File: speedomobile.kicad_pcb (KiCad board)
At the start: 4 copper layers, 100 x 100 mm, 137 parts, among them J1 Conn_01x04, J10 Conn_02x02_Odd_Even, J11 Conn_02x02_Odd_Even, J12 Conn_02x02_Odd_Even, J13 Conn_02x02_Odd_Even, J14 Conn_02x02_Odd_Even, J15 Conn_02x02_Odd_Even, J16 Conn_02x02_Odd_Even, J17 Conn_02x02_Odd_Even, J18 Conn_01x02, J19 Conn_01x02, J2 Conn_01x04, J20 Conn_01x03, J21 Conn_01x03, J22 Conn_01x07, J23 Conn_01x04, J24 Conn_01x03, J25 Conn_01x03, J26 Conn_01x03, J27 Conn_01x02, J28 Conn_01x06, J29 Conn_01x02, J3 Conn_01x04, J30 Conn_01x06, J31 Conn_02x06_Odd_Even, J32 Conn_01x02, J33 Conn_01x03, J34 Conn_01x02, J35 SDCARD_breakout, J36 Conn_01x03, J37 Conn_01x02, J38 Conn_01x03, J4 Conn_01x04, J5 Conn_01x04, J6 Conn_01x04, J7 Conn_01x07, J8 Conn_01x04, J9 Conn_Coaxial, Q1 DMT6012LSS, Q2 DMT6012LSS, Q3 DMT6012LSS, Q4 DMT6012LSS, Q5 BSS138, Q6 BSS138, SW1 SW_Push, U1 MCP1501-33xCH, U10 NEO-M9N, U11 PCF8574, U12 PCF8574, U13 TCA9617A, U2 SC0918, U3 74AHCT367, U4 BTS4140N, U5 CD74HC4067M, U6 MCS1802, U7 MCS1802, U8 V48SD, U9 adafruit_LSM9DS1

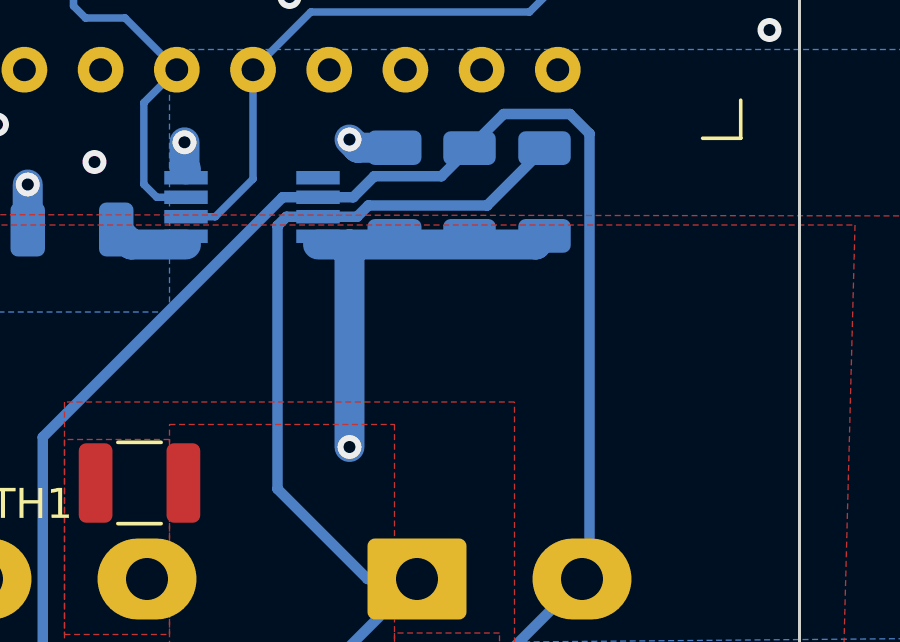
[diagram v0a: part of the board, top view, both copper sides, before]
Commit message: switching to 3v3 i2c
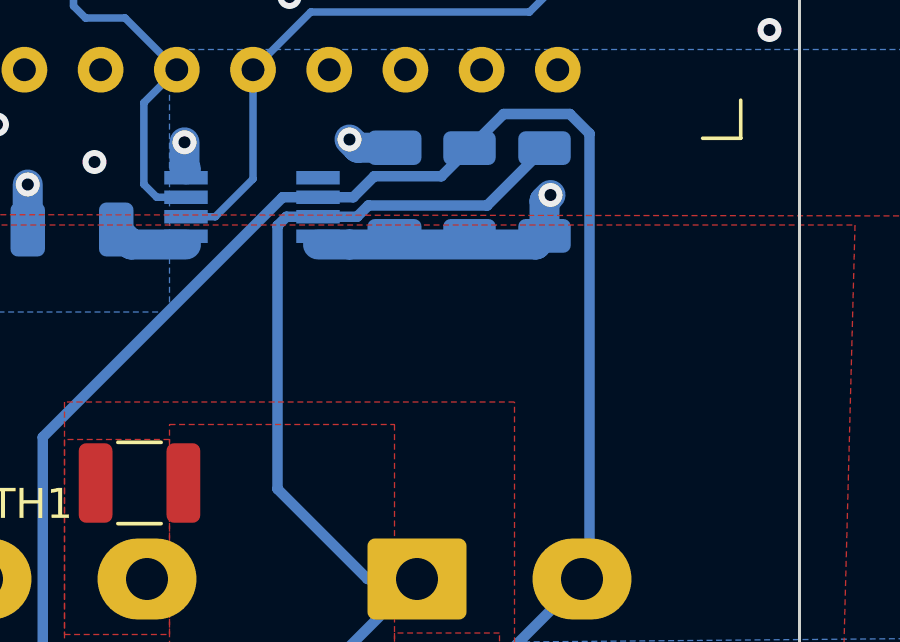
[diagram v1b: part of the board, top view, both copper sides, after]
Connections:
- C24 pad 1: +5V -> +3V3
- R1 pad 1: +5V -> +3V3
- R29 pad 1: +5V -> +3V3
- U13 pad 8: +5V -> +3V3
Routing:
- net +5V: track 21.3 -> 6.87 mm, vias 1 -> 0
- net +3V3: track 219.2 -> 228.3 mm, vias 121 -> 122
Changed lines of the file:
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@@
       (stroke (width 0.1) (type solid)) (layer "B.Fab"))
     (pad "1" smd roundrect (at -1.475 0 90) (size 1.15 1.8) (layers "B.Cu" "B.Paste" "B.Mask") (roundrect_rratio 0.217391)
-      (net 1 "+5V") (pintype "passive"))
+      (net 7 "+3V3") (pintype "passive"))
     (pad "2" smd roundrect (at 1.475 0 90) (size 1.15 1.8) (layers "B.Cu" "B.Paste" "B.Mask") (roundrect_rratio 0.217391)
       (net 6 "GND") (pintype "passive"))
@@
       (stroke (width 0.1) (type solid)) (layer "B.Fab"))
     (pad "1" smd roundrect (at -1.4625 0 90) (size 1.125 1.75) (layers "B.Cu" "B.Paste" "B.Mask") (roundrect_rratio 0.222222)
-      (net 1 "+5V") (pintype "passive"))
+      (net 7 "+3V3") (pintype "passive"))
     (pad "2" smd roundrect (at 1.4625 0 90) (size 1.125 1.75) (layers "B.Cu" "B.Paste" "B.Mask") (roundrect_rratio 0.222222)
       (net 106 "/I2C devices/led ribbon/FAST_SCL_5V") (pintype "passive"))
@@
       (stroke (width 0.1) (type solid)) (layer "B.Fab"))
     (pad "1" smd roundrect (at -1.4625 0 90) (size 1.125 1.75) (layers "B.Cu" "B.Paste" "B.Mask") (roundrect_rratio 0.222222)
-      (net 1 "+5V") (pintype "passive"))
+      (net 7 "+3V3") (pintype "passive"))
     (pad "2" smd roundrect (at 1.4625 0 90) (size 1.125 1.75) (layers "B.Cu" "B.Paste" "B.Mask") (roundrect_rratio 0.222222)
       (net 137 "/I2C devices/led ribbon/FAST_SDA_5V") (pintype "passive"))
@@
       (net 106 "/I2C devices/led ribbon/FAST_SCL_5V") (pinfunction "SCLB") (pintype "bidirectional"))
     (pad "8" smd rect (at 2.2 0.975 90) (size 0.45 1.45) (layers "B.Cu" "B.Paste" "B.Mask")
-      (net 1 "+5V") (pinfunction "VCCB") (pintype "power_in"))
+      (net 7 "+3V3") (pinfunction "VCCB") (pintype "power_in"))
     (model "${KICAD6_3DMODEL_DIR}/Package_SO.3dshapes/VSSOP-8_3.0x3.0mm_P0.65mm.wrl"
       (offset (xyz 0 0 0))
@@
   )
   (segment (start 145.542 110.236) (end 142.367002 110.236) (width 2.2) (layer "F.Cu") (net 1))
-  (via (at 170 69) (size 0.8) (drill 0.4) (layers "F.Cu" "B.Cu") (net 1))
   (segment (start 141.866 110.0035) (end 142.1345 110.0035) (width 1) (layer "B.Cu") (net 1))
   (segment (start 141.3 107.1375) (end 141.3 109.4375) (width 1) (layer "B.Cu") (net 1))
-  (segment (start 170 62.25) (end 168.95 62.25) (width 1) (layer "B.Cu") (net 1))
   (segment (start 141.3 109.4375) (end 141.866 110.0035) (width 1) (layer "B.Cu") (net 1))
-  (segment (start 170 69) (end 170 62.25) (width 1) (layer "B.Cu") (net 1))
   (segment (start 142.367002 110.236) (end 142.240002 110.109) (width 2.2) (layer "B.Cu") (net 1))
   (segment (start 142.1345 110.0035) (end 142.24 110.109) (width 1) (layer "B.Cu") (net 1))
-  (segment (start 176.5 61.9625) (end 176.2125 62.25) (width 1) (layer "B.Cu") (net 1))
-  (segment (start 176.2125 62.25) (end 170 62.25) (width 1) (layer "B.Cu") (net 1))
   (segment (start 120.16 45.63) (end 118.5 45.63) (width 0.25) (layer "B.Cu") (net 2))
   (segment (start 118.5 45.63) (end 115.49 42.62) (width 0.25) (layer "B.Cu") (net 2))
@@
   (via (at 168.1 43.4) (size 0.8) (drill 0.4) (layers "F.Cu" "B.Cu") (net 7))
   (via (at 161.5 59.5) (size 0.8) (drill 0.4) (layers "F.Cu" "B.Cu") (net 7))
+  (via (at 176.7 60.6) (size 0.8) (drill 0.4) (layers "F.Cu" "B.Cu") (net 7))
   (via (at 183.3 52.4) (size 0.8) (drill 0.4) (layers "F.Cu" "B.Cu") (net 7))
   (via (at 153.4 37.9) (size 0.8) (drill 0.4) (layers "F.Cu" "B.Cu") (net 7))
@@
   (via (at 159.5 32.9) (size 0.8) (drill 0.4) (layers "F.Cu" "B.Cu") (net 7))
   (segment (start 132.193621 42.7) (end 134.086828 42.7) (width 0.5) (layer "B.Cu") (net 7))
+  (segment (start 176.5 60.8) (end 176.7 60.6) (width 1) (layer "B.Cu") (net 7))
   (segment (start 122.301 66.04) (end 123.276 66.04) (width 1.8) (layer "B.Cu") (net 7))
   (segment (start 121.329 88.184) (end 120.219625 87.074625) (width 1.8) (layer "B.Cu") (net 7))
@@
   (segment (start 135.025 43.638172) (end 135.025 47.675) (width 0.5) (layer "B.Cu") (net 7))
   (segment (start 107.2 49.2) (end 107.2 46.2) (width 1.8) (layer "B.Cu") (net 7))
+  (segment (start 176.5 61.9625) (end 176.5 60.8) (width 1) (layer "B.Cu") (net 7))
   (segment (start 107.2 46.2) (end 106.6 45.6) (width 1.8) (layer "B.Cu") (net 7))
   (segment (start 108.75 40.25) (end 108.75 40) (width 1.8) (layer "B.Cu") (net 7))
@@
   (segment (start 108.75 41.467284) (end 108.75 40.25) (width 1.8) (layer "B.Cu") (net 7))
   (segment (start 123.276 66.04) (end 128.204 61.112) (width 1.8) (layer "B.Cu") (net 7))
+  (segment (start 170 62.25) (end 168.95 62.25) (width 1) (layer "B.Cu") (net 7))
   (segment (start 135.025 47.675) (end 133.4 49.3) (width 0.5) (layer "B.Cu") (net 7))
   (segment (start 96.46 63.545) (end 95.03 64.975) (width 0.5) (layer "B.Cu") (net 7))
@@
   (segment (start 106 103.4) (end 106 109.8) (width 1.8) (layer "B.Cu") (net 7))
   (segment (start 97.71 52.78) (end 98.42 52.78) (width 1.8) (layer "B.Cu") (net 7))
+  (segment (start 176.5 61.9625) (end 176.2125 62.25) (width 1) (layer "B.Cu") (net 7))
   (segment (start 94.7 95.2) (end 96.025 93.875) (width 1.8) (layer "B.Cu") (net 7))
   (segment (start 106.6 43.617284) (end 108.75 41.467284) (width 1.8) (layer "B.Cu") (net 7))
   (segment (start 91.2 95.2) (end 94.7 95.2) (width 1.8) (layer "B.Cu") (net 7))
+  (segment (start 176.2125 62.25) (end 170 62.25) (width 1) (layer "B.Cu") (net 7))
   (segment (start 141.975 52.95) (end 141.975 50.686918) (width 0.5) (layer "B.Cu") (net 7))
   (segment (start 162.225 61.75) (end 162.725 62.25) (width 1) (layer "B.Cu") (net 7))

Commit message: JLCJLCJLCJLC
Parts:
- removed Q5, Q6: BSS138, Package_TO_SOT_SMD:SOT-23
- removed R21, R22: 4k7, Resistor_SMD:R_1206_3216Metric
- added J39: Conn_02x02_Odd_Even, Connector_Molex:Molex_Mini-Fit_Jr_5566-04A_2x02_P4.20mm_Vertical, B.Cu at (172.3, 65.6)
- added TH4: 7,5A, Resistor_SMD:R_1210_3225Metric, F.Cu at (167.4, 68.3)
- added TH6: 7,5A, Resistor_SMD:R_1210_3225Metric, F.Cu at (172.5, 73.1)
- J36: value Conn_01x03 -> Conn_02x02_Odd_Even; footprint Connector_PinHeader_2.54mm:PinHeader_1x03_P2.54mm_Vertical -> Connector_Molex:Molex_Mini-Fit_Jr_5566-04A_2x02_P4.20mm_Vertical
- J5: value Conn_01x04 -> Conn_01x05; footprint Connector_JST:JST_XH_B4B-XH-A_1x04_P2.50mm_Vertical -> Connector_JST:JST_XH_B5B-XH-A_1x05_P2.50mm_Vertical
- NT3, NT4: footprint NetTie:NetTie-2_SMD_Pad2.0mm -> additional:NetTie-2_SMD_Pad2.0mm-3,6mm
- TH10, TH11, TH12, TH13, TH9: footprint Resistor_SMD:R_1812_4532Metric -> Resistor_SMD:R_1210_3225Metric
- moved J36 75.2 mm to (163.3, 69.8), turned to 90 degrees
- moved J6 12.5 mm to (90.5, 42.8)
- moved C16 10.3 mm to (140.7, 103.5)
- moved J5 7.28 mm to (90.5, 56.2), turned to -90 degrees
- moved TH11 4.91 mm to (158.3, 122.1)
- moved TH12 4.34 mm to (165.5, 122.1)
- moved J10 2.99 mm to (163.2, 80.6)
- moved J11 2.99 mm to (163.2, 91.3)
- moved J12 2.99 mm to (163.2, 101.9)
- moved J13 2.99 mm to (163.2, 112.6)
- moved J15 2.99 mm to (172.2, 87.0)
- moved J17 2.99 mm to (172.2, 108.3)
- moved TH16 2.99 mm to (172.5, 94.6)
- moved TH18 2.99 mm to (172.5, 105.4)
- moved TH3 2.99 mm to (163.0, 83.9)
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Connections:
- J36 pad 1: GND -> /I2C devices/led ribbon/FAST_SCL_5V
- J36 pad 2: GND -> /I2C devices/led ribbon/LED9
- J36 pad 3: Net-(J36-Pin_3) -> /I2C devices/led ribbon/FAST_SDA_5V
- J5 pad 1: +3V3 -> +5VL
- J5 pad 2: /FAST_SDA -> +3V3
- J5 pad 3: /FAST_SCL -> /SDA
- J5 pad 4: GND -> /SCL
- J6 pad 1: +5VL -> +3V3
- J6 pad 2: /I2C devices/SDA_5V -> /SDA
- J6 pad 3: /I2C devices/SCL_5V -> /SCL
- U2 pad 37: Net-(J36-Pin_3) -> unconnected-(U2-3V3_EN-Pad37)
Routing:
- net +3V3: track 228.3 -> 177.2 mm, vias 122 -> 119
- net /SCL: track 140.6 -> 173.7 mm, vias 4 -> 2
- net /SDA: track 135.4 -> 163.7 mm, vias 4 -> 2
- net /FAST_SCL: track 181.0 -> 154.0 mm
- net Net-(J36-Pin_3): track 24.5 -> 0.00 mm
- net /FAST_SDA: track 167.4 -> 143.2 mm
- net /I2C devices/led ribbon/FAST_SDA_5V: track 122.8 -> 137.0 mm
- net /I2C devices/SCL_5V: track 9.72 -> 0.00 mm
- net /I2C devices/SDA_5V: track 9.29 -> 0.00 mm
- net /I2C devices/led ribbon/FAST_SCL_5V: track 102.6 -> 111.1 mm
- net /power/PWR2_PWM_ON: track 42.6 -> 37.3 mm, vias 1 -> 0
- net /UART: track 71.7 -> 75.5 mm, vias 0 -> 2
- net /ADC: track 58.3 -> 54.5 mm, vias 3 -> 1
- net +5V: track 6.87 -> 9.71 mm, vias 0 -> 7
- net /power/PWR1_PWM_ON: track 30.4 -> 27.7 mm
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- added copper zone on F.Cu, net /I2C devices/led ribbon/LED10
- added copper zone on F.Cu, net /I2C devices/led ribbon/LED9
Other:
- board text added: "5V-7.5A I2C"
- board text added: "5V40A"
- board text added: "I2C Expansion"
- board text added: "JLCJLCJLCJLC"
- board text added: "LCD+RFID"
- board text removed: "5V 40A"
- board text removed: "5V-3A I2C"
- board text removed: "LCD"
- board text removed: "RFID"

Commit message: 2 layers!
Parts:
- removed NT1: NetTie_2, NetTie:NetTie-2_SMD_Pad0.5mm
- removed NT3, NT4: NetTie_2, additional:NetTie-2_SMD_Pad2.0mm-3,6mm
- removed Q3, Q4: DMT6012LSS, Package_SO:SOIC-8_3.9x4.9mm_P1.27mm
- removed R14, R15: 1k, Resistor_SMD:R_1206_3216Metric
- removed R16, R17: 190k, Resistor_SMD:R_1206_3216Metric
- C13, C15, C16: moved to B.Cu
- J20, J21: value Conn_01x03 -> Conn_01x02; footprint Connector_JST:JST_XH_B3B-XH-A_1x03_P2.50mm_Vertical -> Connector_JST:JST_XH_B2B-XH-A_1x02_P2.50mm_Vertical
- moved R2 29.1 mm to (118.8, 69.3)
- moved D1 27.9 mm to (131.9, 101.7), turned to 45 degrees
- moved C13 17.9 mm to (129.1, 113.5), turned to -90 degrees
- moved C15 17.9 mm to (132.6, 113.5), turned to -90 degrees
- moved C16 17.9 mm to (125.8, 113.5), turned to -90 degrees
- moved J29 16.9 mm to (136.8, 126.9), turned to 90 degrees
- moved R6 11.6 mm to (117.3, 121.1), turned to 90 degrees
- moved Q1 10.2 mm to (134.3, 118.6)
- moved J27 9.63 mm to (151.0, 94.1)
- moved Q2 9.57 mm to (123.0, 126.2)
- moved R7 9.22 mm to (121.8, 110.6)
- moved R4 9.20 mm to (131.6, 123.7), turned to 90 degrees
- moved R3 8.98 mm to (129.3, 125.5), turned to -90 degrees
- moved R5 7.69 mm to (119.6, 121.1), turned to -90 degrees
- moved J21 7.53 mm to (154.7, 123.2)
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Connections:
- J10 pad 4: GNDPWR -> GND
- J11 pad 4: GNDPWR -> GND
- J12 pad 4: GNDPWR -> GND
- J13 pad 4: GNDPWR -> GND
- J14 pad 4: GNDPWR -> GND
- J15 pad 4: GNDPWR -> GND
- J16 pad 4: GNDPWR -> GND
- J17 pad 4: GNDPWR -> GND
- J18 pad 2: GNDPWR -> GND
- J19 pad 2: GNDPWR -> GND
- J20 pad 1: /power/PWR2 -> /power/PWR1
- J20 pad 2: /power/PWR2_PWM_ON -> GND
- J21 pad 1: /power/PWR1 -> /power/PWR2
- J21 pad 2: /power/PWR1_PWM_ON -> GND
- J31 pad 2: /GPIO0 -> GND
- J31 pad 3: /GPIO1 -> /GPIO0
- J31 pad 4: /GPIO2 -> /GPIO1
- J31 pad 5: /GPIO3 -> /GPIO2
- J31 pad 6: GND -> /GPIO3
- J36 pad 4: GNDPWR -> GND
- J39 pad 4: GNDPWR -> GND
- U2 pad 26: /PWR2_PWM -> unconnected-(U2-I2C0SDA/GP20-Pad26)
- U2 pad 27: /PWR1_PWM -> unconnected-(U2-I2C0SCL/GP21-Pad27)
- U8 pad 7: Net-(U8-Sense+) -> +5VL
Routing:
- net +3V3: track 177.2 -> 446.1 mm, vias 119 -> 7
- net /PWR2_PWM: track 99.3 -> 0.00 mm
- net /PWR1_PWM: track 97.6 -> 0.00 mm, vias 1 -> 0
- net +5VL: track 178.2 -> 249.5 mm, vias 4 -> 3
- net /power/PWR2_PWM_ON: track 37.3 -> 0.00 mm
- net /TSDZ2_RX: track 72.5 -> 106.4 mm
- net /TSDZ2_RX_5V: track 36.6 -> 3.27 mm
- net /power/PWR1_PWM_ON: track 27.7 -> 0.00 mm
- net Net-(Q4-G): track 18.3 -> 0.00 mm
- net +5V: track 9.71 -> 26.9 mm, vias 7 -> 5
- net +48V: track 26.0 -> 42.6 mm
- net Net-(Q3-G): track 14.3 -> 0.00 mm
- net Net-(U8-Sense+): track 13.0 -> 0.00 mm
- net /FAST_SDA: track 143.2 -> 155.1 mm, vias 1 -> 3
- net Net-(Q1-G): track 7.24 -> 19.1 mm
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- removed copper zone on B.Cu, net +5VL
- removed copper zone on In1.Cu, net GND
- removed copper zone on In2.Cu, net GND
- removed copper zone on B.Cu, net GNDPWR
- removed copper zone on F.Cu, net GNDPWR
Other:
- copper layers 4 -> 2

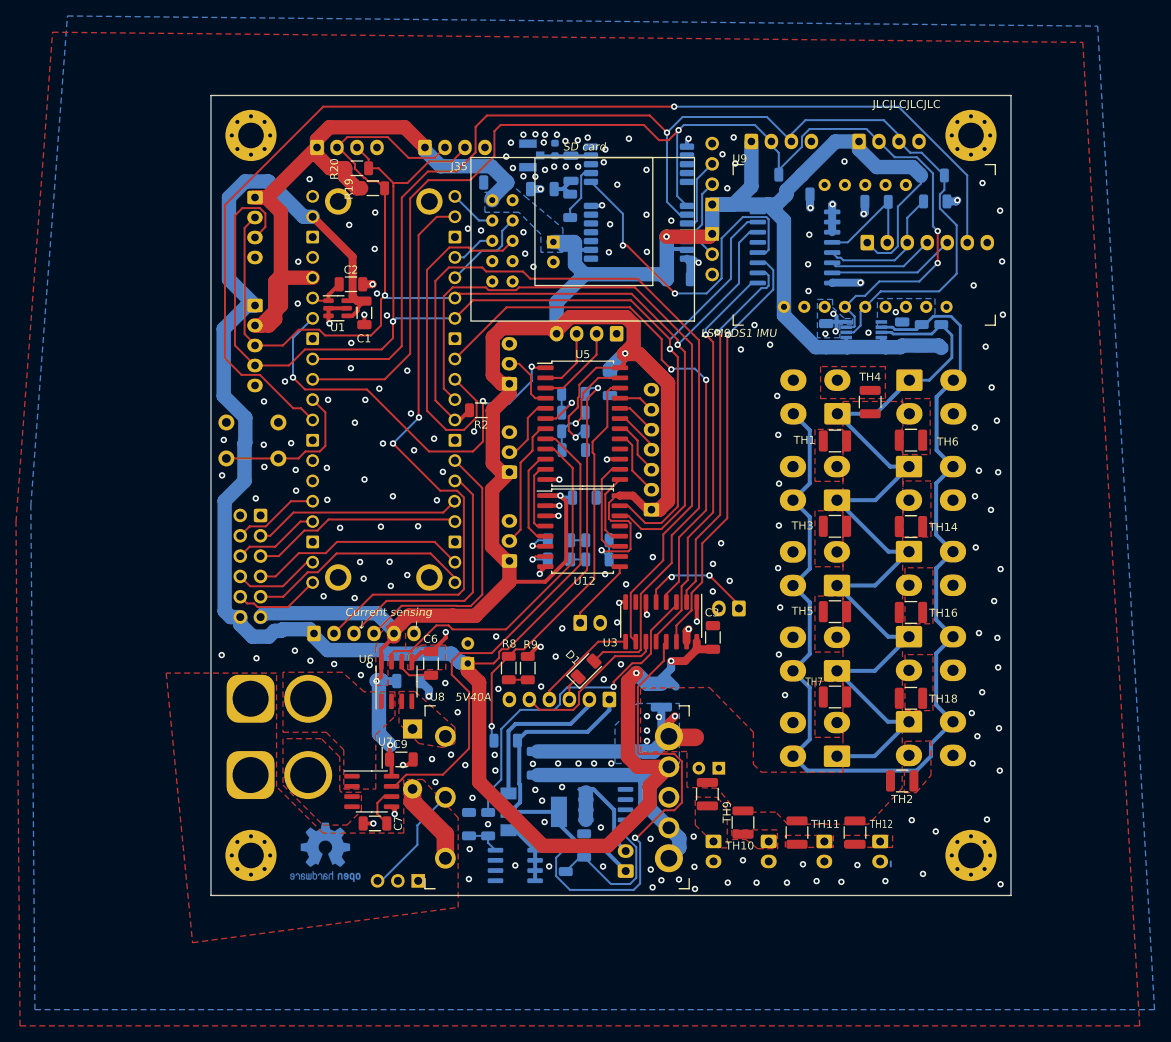
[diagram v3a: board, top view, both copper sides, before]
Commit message: 2 layer better ground plane
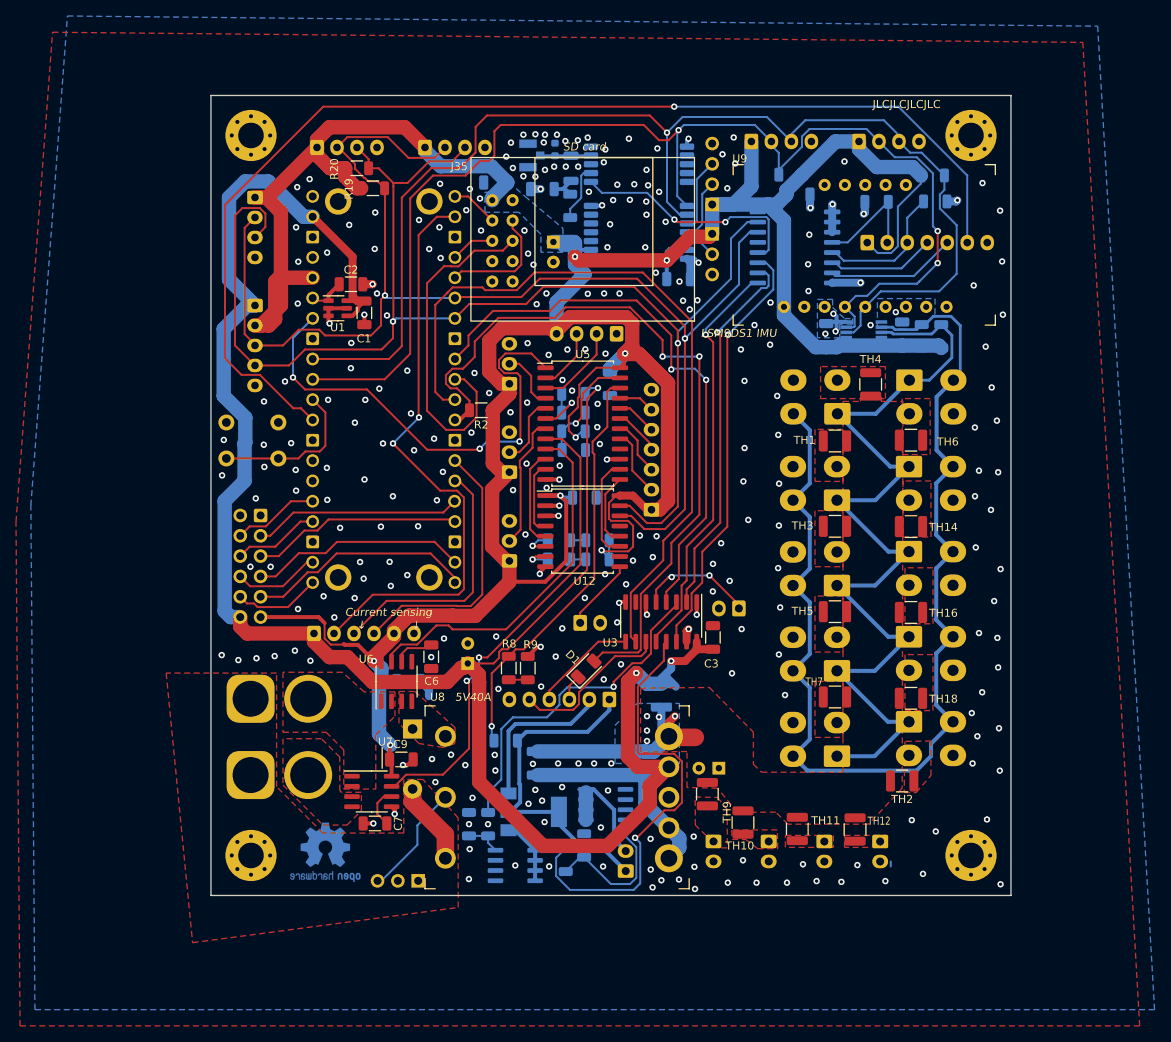
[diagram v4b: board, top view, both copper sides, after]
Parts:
- moved TH4 2.21 mm to (167.5, 66.1)
- moved C6 0.84 mm to (112.5, 100.2), turned to -90 degrees
- moved TH11 0.45 mm to (158.3, 121.7)
- moved TH12 0.39 mm to (165.5, 121.7)
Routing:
- net /I2C devices/RESET_M9N: track 42.6 -> 30.0 mm
- net /TSDZ2_RX: track 106.4 -> 94.7 mm, vias 0 -> 2
- net /ADC: track 52.5 -> 60.1 mm
- net GND: track 86.8 -> 79.9 mm, vias 224 -> 285
- net /TSDZ2_TX: track 88.8 -> 93.8 mm
- net /MOSI: track 11.2 -> 14.9 mm
- net +3V3: track 446.1 -> 443.0 mm, vias 7 -> 8
- net /Imotor: track 62.8 -> 60.1 mm, vias 0 -> 2
- net /VSPEED: track 69.3 -> 71.7 mm
- net /SDA: track 165.8 -> 168.0 mm
- net +5VL: track 249.5 -> 251.2 mm
- net /SCL: track 173.2 -> 174.7 mm
- net /CS_SD: track 43.8 -> 43.2 mm
- removed copper zone on F.Cu, net +3V3
